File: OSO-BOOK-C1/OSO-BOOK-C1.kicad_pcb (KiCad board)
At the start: 2 copper layers, 85 x 115 mm, 39 parts, among them J1 JST-PH3, J2 JST-PH3, J3 JST-PH4, Q1 Q_PMOS_GSD, Q2 Q_PMOS_GSD, SW1 SW_SPDT, U1 Pico, U2 OSO-BOOK-C2-01, U3 MEM2075, U4 GD25Q16C

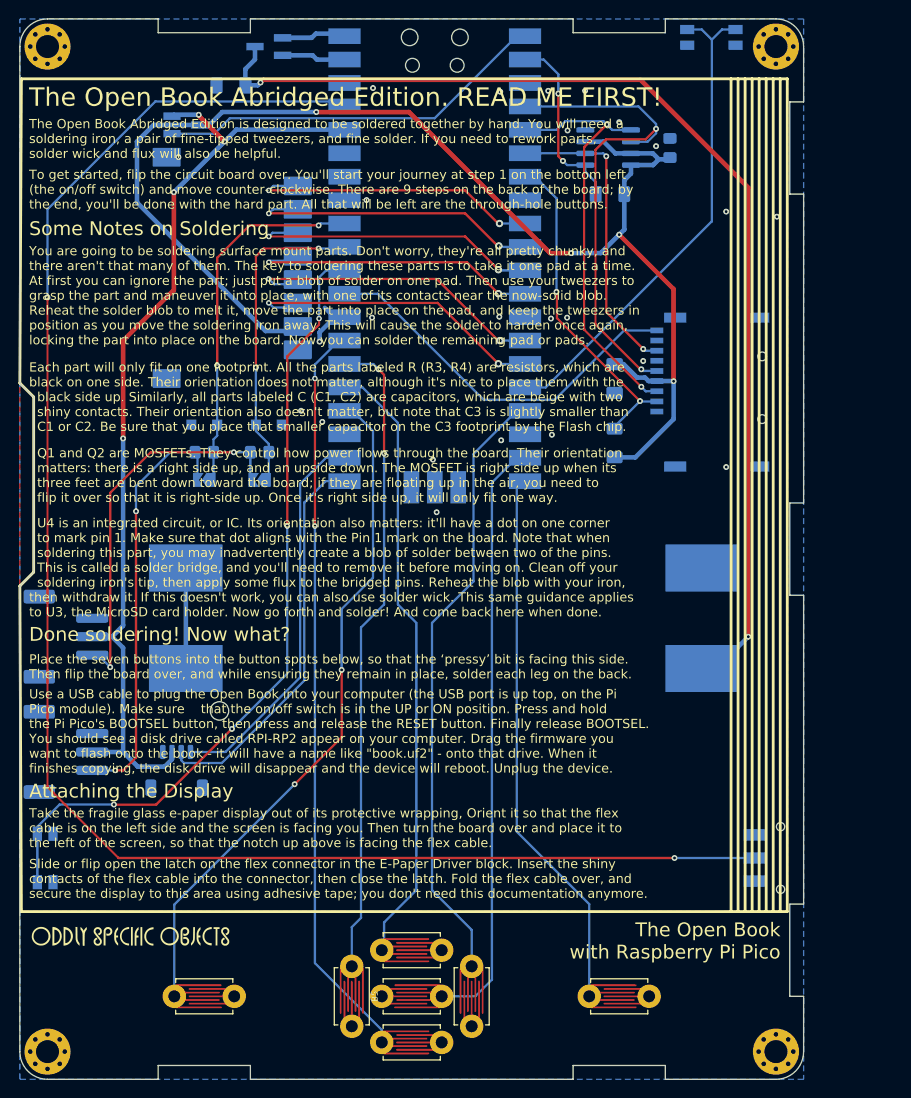
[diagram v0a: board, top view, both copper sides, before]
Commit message: rev 5: remove zener diodes, silkscreen tweaks
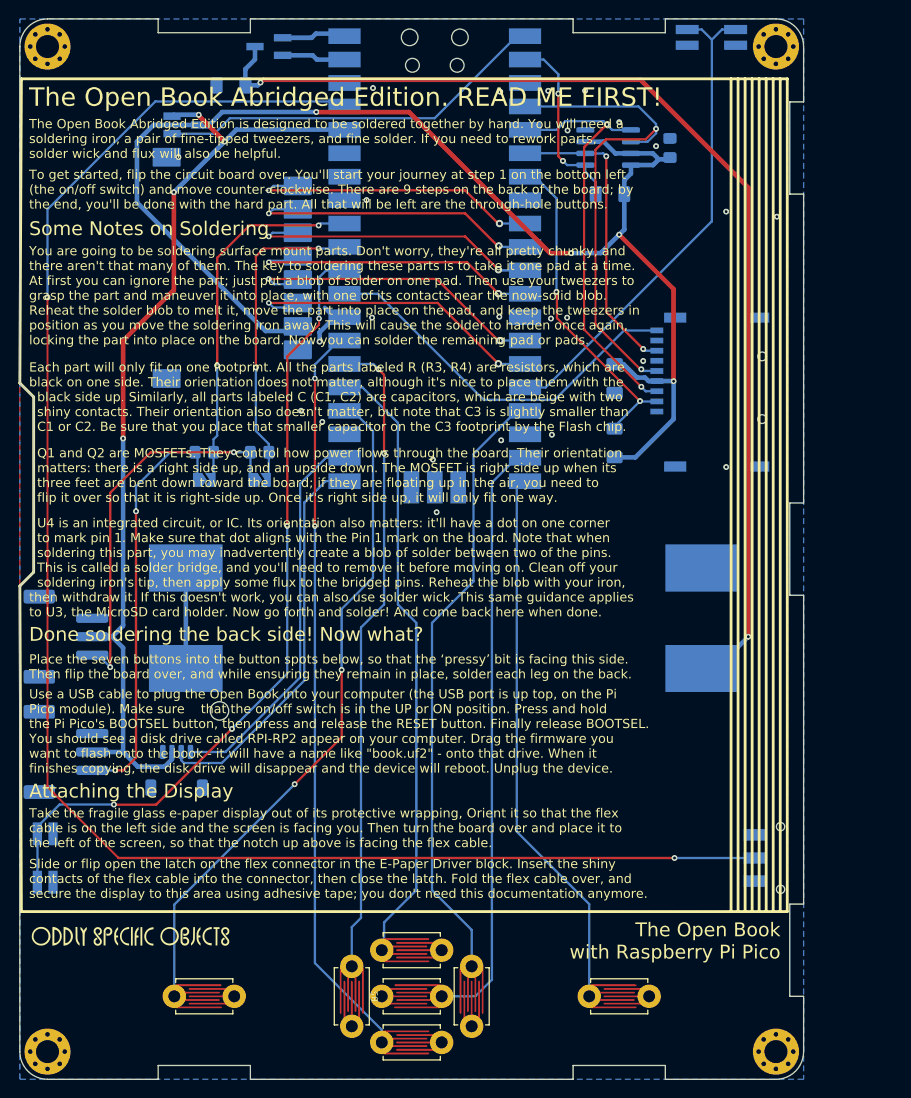
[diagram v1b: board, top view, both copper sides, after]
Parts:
- removed D1, D2: D_Zener, Diode_SMD:D_SOD-123F
- turned JP1 to 0 degrees
- turned JP2 to 0 degrees
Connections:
- BT1 pad 3: BATT_MID -> (no net)
- J1 pad 1: Net-(J1-Pad1) -> /_GP26
- J2 pad 1: Net-(J2-Pad1) -> /_GP27
- JP1 pad 1: /GP26 -> /_GP26
- JP1 pad 2: Net-(J1-Pad1) -> /GP26
- JP2 pad 1: /GP27 -> /_GP27
- JP2 pad 2: Net-(J2-Pad1) -> /GP27
- R1 pad 2: Net-(J1-Pad1) -> /_GP26
- R2 pad 2: Net-(J2-Pad1) -> /_GP27
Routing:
- net Net-(J2-Pad1): track 45.8 -> 0.00 mm, vias 2 -> 0
- net /_GP27: track 0.00 -> 45.8 mm, vias 0 -> 2
- net Net-(J1-Pad1): track 41.1 -> 0.00 mm, vias 2 -> 0
- net /_GP26: track 0.00 -> 41.1 mm, vias 0 -> 2
- net BATT_MID: track 10.9 -> 0.00 mm
- net (no net): track 0.00 -> 10.9 mm
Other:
- board text added: "Alignment matters here! Pin 1 of the chip has a dot. Align the dot to the Pin 1 arrow at the bottom right. Solder all pins, as well as R3 and C3."
- board text added: "Done soldering the back side! Now what?"
- board text added: "OSO-BOOK-C1-05"
- board text added: "Place R1/R2 for current limiting on J1/J2 (i.e. to drive an LED), OR bridge JP1/JP2 closed to use without pro- tection (i.e. for a button or switch)."
- board text added: "Starting with C1, melt a blob of solder on one pad, then use your tweezers to move the part into place while the solder is molten. Ensure part alignment. Then solder the other pad or pads."
- board text added: "Tape flex cable here."
- board text removed: "Done soldering! Now what?"
- board text removed: "Feel free to ignore parts D1, D2, R1 & R2, unless you plan to add STEMMA ports J1 & J2 (to use GP26 or GP27)."
- board text removed: "OSO-BOOK-C1-04"
- board text removed: "Solder pin 1 (marked by a dot on the chip) to pin 1 here. Move the chip until aligned, then solder all pins as well as R3 & C3."
- board text removed: "Starting with C1, melt a blob of solder on one pad, then use your tweezers to move the part into place while the solder is molten. Then solder the other pad or pads."
- board text removed: "These parts offer current limiting and overvoltage protection for J1&J2, although you can omit them and solder JP1 or JP2 closed to use J1 or J2 without protection."

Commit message: rev 06
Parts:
- added G***: LOGO, LOGO, B.Cu at (61.2, 101.2)
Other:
- board text added: "OSO-BOOK-C1-06"
- board text added: "SDA: GP16 SCL: GP17"
- board text added: "STEMMA-QT:"
- board text added: "Sponsored by"
- board text removed: "OSO-BOOK-C1-05"
